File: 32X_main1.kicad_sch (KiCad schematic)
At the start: 17 parts, among them IC5041 315-5818-A, IC505 315-5805, IC509 74AC04

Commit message: Start PCB layout.
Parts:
- removed IC5041: 315-5818-A, symbol 32X:315-5818-A
- added IC504: 315-5818, Package_QFP:LQFP-176_24x24mm_P0.5mm, symbol 32X:315-5818
- C5: footprint (none) -> Capacitor_SMD:C_0805_2012Metric
- IC505: footprint (none) -> Package_QFP:PQFP-80_14x20mm_P0.8mm
- IC509: footprint (none) -> Package_SO:SO-14_3.9x8.65mm_P1.27mm
- R561, R562, R566: footprint (none) -> Resistor_SMD:R_0805_2012Metric
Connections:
- net CTD0: now also IC504.159 (RD0)
- net CTD1: now also IC504.160 (RD1)
- net CTD10: now also IC504.169 (RD10)
- net CTD11: now also IC504.170 (RD11)
- net CTD12: now also IC504.171 (RD12)
- net CTD13: now also IC504.172 (RD13)
- net CTD14: now also IC504.173 (RD14)
- net CTD15: now also IC504.174 (RD15)
- net CTD2: now also IC504.161 (RD2)
- net CTD3: now also IC504.162 (RD3)
- net CTD4: now also IC504.163 (RD4)
- net CTD5: now also IC504.164 (RD5)
- net CTD6: now also IC504.165 (RD6)
- net CTD7: now also IC504.166 (RD7)
- net CTD8: now also IC504.167 (RD8)
- net CTD9: now also IC504.168 (RD9)
- net GND: now also IC504.152 (CHPLL), IC504.153 (BUNRI), IC504.8 (KILL)
- net GNDA: now also IC504.130 (AGND)
- net PCH0: now also IC504.2 (CH0)
- net PCH1: now also IC504.3 (CH1)
- net VA1: now also IC504.84 (VA1)
- net VA10: now also IC504.75 (VA10)
- net VA11: now also IC504.74 (VA11)
- net VA12: now also IC504.73 (VA12)
- net VA13: now also IC504.72 (VA13)
- net VA14: now also IC504.71 (VA14)
- net VA15: now also IC504.70 (VA15)
- net VA16: now also IC504.69 (VA16)
- net VA17: now also IC504.68 (VA17)
- net VA18: now also IC504.67 (VA18)
- net VA19: now also IC504.101 (VA19)
- net VA2: now also IC504.83 (VA2)
- net VA20: now also IC504.102 (VA20)
- net VA21: now also IC504.103 (VA21)
- net VA22: now also IC504.104 (VA22)
- net VA23: now also IC504.105 (VA23)
- net VA3: now also IC504.82 (VA3)
- net VA4: now also IC504.81 (VA4)
- net VA5: now also IC504.80 (VA5)
- net VA6: now also IC504.79 (VA6)
- net VA7: now also IC504.78 (VA7)
- net VA8: now also IC504.77 (VA8)
- net VA9: now also IC504.76 (VA9)
- net VD0: now also IC504.86 (VD0)
- net VD1: now also IC504.92 (VD1)
- net VD10: now also IC504.96 (VD10)
- net VD11: now also IC504.99 (VD11)
- net VD12: now also IC504.117 (VD12)
- net VD13: now also IC504.116 (VD13)
- net VD14: now also IC504.115 (VD14)
- net VD15: now also IC504.114 (VD15)
- net VD2: now also IC504.95 (VD2)
- net VD3: now also IC504.98 (VD3)
- net VD4: now also IC504.97 (VD4)
- net VD5: now also IC504.94 (VD5)
- net VD6: now also IC504.91 (VD6)
- net VD7: now also IC504.85 (VD7)
- net VD8: now also IC504.90 (VD8)
- net VD9: now also IC504.93 (VD9)
- net ~{CART}: now also IC504.7 (~{CART})
- net ~{CAS0}: now also IC504.106 (~{CAS0})
- net ~{CAS2}: now also IC504.113 (~{CAS2})
- net ~{CASEL}: now also IC504.155 (~{OASEL})
- net ~{CCAS0}: now also IC504.157 (~{OCAS0})
- net ~{CCAS2}: now also IC504.156 (~{OCAS2})
- net ~{CCE0}: now also IC504.154 (~{OCE0})
- net ~{CE0}: now also IC504.107 (~{CE0})
- net ~{CLWR}: now also IC504.158 (~{OLWE})
- net ~{DTAK}: now also IC504.109 (~{DTAK})
- net ~{LWR}: now also IC504.120 (~{LWR})
- net ~{UWR}: now also IC504.121 (~{UWR})
- net ~{VRES}: now also IC504.119 (~{VRES})
- net ~{XRESET}: now also IC504.100 (~{MRES})
- net at FB7.2: now also IC504.108 (~{AS})
- net at FB7.2: now also IC504.112 (VCLK)
- net at FB7.2: now also IC504.118 (~{ASEL})
- net at C5.1, C5.1, L501.2: now also IC504.129 (AVDD)
- net at IC505.58 (~{SEL}): now also IC504.151 (~{SEL})
- net at FB7.1: now also IC504.33 (CKIO)
- net at IC505.10 (OVA19): now also IC504.4 (OVA19)
- net at IC505.9 (OVA20): now also IC504.5 (OVA20)
- net at IC505.8 (OVA21): now also IC504.6 (OVA21)
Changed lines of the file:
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@@
       (effects (font (size 1.27 1.27)) (justify right))
     )
-    (property "Footprint" "" (at 222.123 232.41 90)
+    (property "Footprint" "Resistor_SMD:R_0805_2012Metric" (at 222.123 232.41 90)
       (effects (font (size 1.27 1.27)) hide)
     )
@@
       (effects (font (size 1.27 1.27)))
     )
-    (property "Footprint" "" (at 135.89 237.49 0)
+    (property "Footprint" "Package_SO:SO-14_3.9x8.65mm_P1.27mm" (at 135.89 237.49 0)
       (effects (font (size 1.27 1.27)) hide)
     )
@@
     )
   )
-  (symbol (lib_id "32X:315-5818-A") (at 176.53 48.26 0) (unit 1)
-    (in_bom yes) (on_board yes) (dnp no)
-    (property "Reference" "IC5041" (at 176.53 43.815 0)
-      (effects (font (size 1.27 1.27)))
-    )
-    (property "Value" "315-5818-A" (at 176.53 46.355 0)
-      (effects (font (size 1.27 1.27)))
-    )
-    (property "Footprint" "" (at 176.53 83.82 0)
-      (effects (font (size 1.27 1.27)) hide)
-    )
-    (property "Datasheet" "" (at 176.53 83.82 0)
-      (effects (font (size 1.27 1.27)) hide)
-    )
-    (pin "100")
-    (pin "101")
-    (pin "102")
-    (pin "103")
-    (pin "104")
-    (pin "105")
-    (pin "106")
-    (pin "107")
-    (pin "108")
-    (pin "109")
-    (pin "112")
-    (pin "113")
-    (pin "114")
-    (pin "115")
-    (pin "116")
-    (pin "117")
-    (pin "118")
-    (pin "119")
-    (pin "120")
-    (pin "121")
-    (pin "128")
-    (pin "129")
-    (pin "130")
-    (pin "151")
-    (pin "152")
-    (pin "153")
-    (pin "154")
-    (pin "155")
-    (pin "156")
-    (pin "157")
-    (pin "158")
-    (pin "159")
-    (pin "160")
-    (pin "161")
-    (pin "162")
-    (pin "163")
-    (pin "164")
-    (pin "165")
-    (pin "166")
-    (pin "167")
-    (pin "168")
-    (pin "169")
-    (pin "170")
-    (pin "171")
-    (pin "172")
-    (pin "173")
-    (pin "174")
-    (pin "2")
-    (pin "3")
-    (pin "33")
-    (pin "4")
-    (pin "5")
-    (pin "6")
-    (pin "67")
-    (pin "68")
-    (pin "69")
-    (pin "7")
-    (pin "70")
-    (pin "71")
-    (pin "72")
-    (pin "73")
-    (pin "74")
-    (pin "75")
-    (pin "76")
-    (pin "77")
-    (pin "78")
-    (pin "79")
-    (pin "8")
-    (pin "80")
-    (pin "81")
-    (pin "82")
-    (pin "83")
-    (pin "84")
-    (pin "85")
-    (pin "86")
-    (pin "90")
-    (pin "91")
-    (pin "92")
-    (pin "93")
-    (pin "94")
-    (pin "95")
-    (pin "96")
-    (pin "97")
-    (pin "98")
-    (pin "99")
-    (instances
-      (project "Neptune"
-        (path "/bcc23b51-b742-4ae5-9dd6-d96a24058944/a9caee2e-423b-443e-a11f-5841882e2685"
-          (reference "IC5041") (unit 1)
-        )
-      )
-    )
-  )
   (symbol (lib_id "power:GND") (at 291.465 178.435 0) (unit 1)
     (in_bom yes) (on_board yes) (dnp no) (fields_autoplaced)
@@
       (effects (font (size 1.27 1.27)) (justify left))
     )
-    (property "Footprint" "" (at 257.81 251.46 0)
+    (property "Footprint" "Package_SO:SO-14_3.9x8.65mm_P1.27mm" (at 257.81 251.46 0)
       (effects (font (size 1.27 1.27)) hide)
     )
@@
       (effects (font (size 1.27 1.27)) (justify left))
     )
-    (property "Footprint" "" (at 195.9102 187.325 0)
+    (property "Footprint" "Capacitor_SMD:C_0805_2012Metric" (at 195.9102 187.325 0)
       (effects (font (size 1.27 1.27)) hide)
     )
@@
       (effects (font (size 1.27 1.27)) (justify left))
     )
-    (property "Footprint" "" (at 292.4302 165.1 0)
+    (property "Footprint" "Capacitor_SMD:C_0805_2012Metric" (at 292.4302 165.1 0)
       (effects (font (size 1.27 1.27)) hide)
     )
@@
       (effects (font (size 1.27 1.27)) (justify left))
     )
-    (property "Footprint" "" (at 273.3802 165.1 0)
+    (property "Footprint" "Capacitor_SMD:C_0805_2012Metric" (at 273.3802 165.1 0)
       (effects (font (size 1.27 1.27)) hide)
     )
@@
       (effects (font (size 1.27 1.27)) (justify left))
     )
-    (property "Footprint" "" (at 283.5402 165.1 0)
+    (property "Footprint" "Capacitor_SMD:C_0805_2012Metric" (at 283.5402 165.1 0)
       (effects (font (size 1.27 1.27)) hide)
     )
@@
       (effects (font (size 1.27 1.27)))
     )
-    (property "Footprint" "" (at 156.845 237.49 0)
+    (property "Footprint" "Package_SO:SO-14_3.9x8.65mm_P1.27mm" (at 156.845 237.49 0)
       (effects (font (size 1.27 1.27)) hide)
     )
@@
       (effects (font (size 1.27 1.27)))
     )
-    (property "Footprint" "" (at 118.11 156.845 0)
+    (property "Footprint" "Package_SO:SO-14_3.9x8.65mm_P1.27mm" (at 118.11 156.845 0)
       (effects (font (size 1.27 1.27)) hide)
     )
@@
       (effects (font (size 1.27 1.27)))
     )
-    (property "Footprint" "" (at 146.685 225.933 90)
+    (property "Footprint" "Resistor_SMD:R_0805_2012Metric" (at 146.685 225.933 90)
       (effects (font (size 1.27 1.27)) hide)
     )
@@
       (effects (font (size 1.27 1.27)))
     )
-    (property "Footprint" "" (at 117.475 239.268 90)
+    (property "Footprint" "Resistor_SMD:R_0805_2012Metric" (at 117.475 239.268 90)
       (effects (font (size 1.27 1.27)) hide)
     )
@@
       (effects (font (size 1.27 1.27)))
     )
-    (property "Footprint" "" (at 249.555 83.82 0)
+    (property "Footprint" "Package_QFP:PQFP-80_14x20mm_P0.8mm" (at 249.555 83.82 0)
       (effects (font (size 1.27 1.27)) hide)
     )
@@
       (effects (font (size 1.27 1.27)) (justify left))
     )
-    (property "Footprint" "" (at 204.8002 187.325 0)
+    (property "Footprint" "Capacitor_SMD:C_0805_2012Metric" (at 204.8002 187.325 0)
       (effects (font (size 1.27 1.27)) hide)
     )
@@
       (effects (font (size 1.27 1.27)))
     )
-    (property "Footprint" "" (at 249.555 203.2 0)
+    (property "Footprint" "Package_SO:SO-14_3.9x8.65mm_P1.27mm" (at 249.555 203.2 0)
       (effects (font (size 1.27 1.27)) hide)
     )
@@
         )
       )
+    )
+  )
+  (symbol (lib_id "32X:315-5818") (at 176.53 48.26 0) (unit 1)
+    (in_bom yes) (on_board yes) (dnp no) (fields_autoplaced)
+    (property "Reference" "IC504" (at 176.53 43.18 0)
+      (effects (font (size 1.27 1.27)))
+    )
+    (property "Value" "315-5818" (at 176.53 45.72 0)
+      (effects (font (size 1.27 1.27)))
+    )
+    (property "Footprint" "Package_QFP:LQFP-176_24x24mm_P0.5mm" (at 176.53 48.26 0)
+      (effects (font (size 1.27 1.27)) hide)
+    )
+    (property "Datasheet" "" (at 176.53 48.26 0)
+      (effects (font (size 1.27 1.27)) hide)
+    )
+    (pin "100")
+    (pin "101")
+    (pin "102")
+    (pin "103")
+    (pin "104")
+    (pin "105")
+    (pin "106")
+    (pin "107")
+    (pin "108")
+    (pin "109")
+    (pin "112")
+    (pin "113")
+    (pin "114")
+    (pin "115")
+    (pin "116")
+    (pin "117")
+    (pin "118")
+    (pin "119")
+    (pin "120")
+    (pin "121")
+    (pin "128")
+    (pin "129")
+    (pin "130")
+    (pin "151")
+    (pin "152")
+    (pin "153")
+    (pin "154")
+    (pin "155")
+    (pin "156")
+    (pin "157")
+    (pin "158")
+    (pin "159")
+    (pin "160")
+    (pin "161")
+    (pin "162")
+    (pin "163")
+    (pin "164")
+    (pin "165")
+    (pin "166")
+    (pin "167")
+    (pin "168")
+    (pin "169")
+    (pin "170")
+    (pin "171")
+    (pin "172")
+    (pin "173")
+    (pin "174")
+    (pin "2")
+    (pin "3")
+    (pin "33")
+    (pin "4")
+    (pin "5")
+    (pin "6")
+    (pin "67")
+    (pin "68")
+    (pin "69")
+    (pin "7")
+    (pin "70")
+    (pin "71")
+    (pin "72")
+    (pin "73")
+    (pin "74")
+    (pin "75")
+    (pin "76")
+    (pin "77")
+    (pin "78")
+    (pin "79")
+    (pin "8")
+    (pin "80")
+    (pin "81")
+    (pin "82")
+    (pin "83")
+    (pin "84")
+    (pin "85")
+    (pin "86")
+    (pin "90")
+    (pin "91")
+    (pin "92")
+    (pin "93")
+    (pin "94")
+    (pin "95")
+    (pin "96")
+    (pin "97")
+    (pin "98")
+    (pin "99")
+    (pin "1")
+    (pin "10")
+    (pin "11")
+    (pin "110")
+    (pin "111")
+    (pin "12")
+    (pin "122")
+    (pin "123")
+    (pin "124")
+    (pin "125")
+    (pin "126")
+    (pin "127")
+    (pin "13")
+    (pin "131")
+    (pin "132")
+    (pin "133")
+    (pin "134")
+    (pin "135")
+    (pin "136")
+    (pin "137")
+    (pin "138")
+    (pin "139")
+    (pin "14")
+    (pin "140")
+    (pin "141")
+    (pin "142")
+    (pin "143")
+    (pin "144")
+    (pin "145")
+    (pin "146")
+    (pin "147")
+    (pin "148")
+    (pin "149")
+    (pin "15")
+    (pin "150")
+    (pin "16")
+    (pin "17")
+    (pin "175")
+    (pin "176")
+    (pin "18")
+    (pin "19")
+    (pin "20")
+    (pin "21")
+    (pin "22")
+    (pin "23")
+    (pin "24")
+    (pin "25")
+    (pin "26")
+    (pin "27")
+    (pin "28")
+    (pin "29")
+    (pin "30")
+    (pin "31")
+    (pin "32")
+    (pin "34")
+    (pin "35")
+    (pin "36")
+    (pin "37")
+    (pin "38")
+    (pin "39")
+    (pin "40")
+    (pin "41")
+    (pin "42")
+    (pin "43")
+    (pin "44")
+    (pin "45")
+    (pin "46")
+    (pin "47")
+    (pin "48")
+    (pin "49")
+    (pin "50")
+    (pin "51")
+    (pin "52")
+    (pin "53")
+    (pin "54")
+    (pin "55")
+    (pin "56")
+    (pin "57")
+    (pin "58")
+    (pin "59")
+    (pin "60")
+    (pin "61")
+    (pin "62")
+    (pin "63")
+    (pin "64")
+    (pin "65")
+    (pin "66")
+    (pin "87")
+    (pin "88")
+    (pin "89")
+    (pin "9")
+    (instances
+      (project "Neptune"
+        (path "/bcc23b51-b742-4ae5-9dd6-d96a24058944/a9caee2e-423b-443e-a11f-5841882e2685"
+          (reference "IC504") (unit 1)
+        )
+      )

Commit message: Save first mock-up before updating footprints.
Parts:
- FB7, L501: footprint (none) -> Inductor_SMD:L_0805_2012Metric
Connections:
- net GND renamed GND2
- net GNDA renamed GNDA2
- net PCH0 renamed PCM0
- net PCH1 renamed PCM1

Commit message: Draft new layout with more accurate footprints.
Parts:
- C5: footprint Capacitor_SMD:C_0805_2012Metric -> Capacitor_SMD:C_1206_3216Metric
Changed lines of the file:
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@@
       (effects (font (size 1.27 1.27)) (justify left))
     )
-    (property "Footprint" "Capacitor_SMD:C_0805_2012Metric" (at 292.4302 165.1 0)
+    (property "Footprint" "Capacitor_SMD:C_1206_3216Metric" (at 292.4302 165.1 0)
       (effects (font (size 1.27 1.27)) hide)
     )
@@
       (effects (font (size 1.27 1.27)) (justify left))
     )
-    (property "Footprint" "Capacitor_SMD:C_0805_2012Metric" (at 204.8002 187.325 0)
-      (effects (font (size 1.27 1.27)) hide)
-    )
+    (property "Footprint" "Capacitor_SMD:C_1206_3216Metric" (at 204.8002 187.325 0)
+      (effects (font (size 1.27 1.27)) hide)
+    )

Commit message: Fill zones, DRC fixes.
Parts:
- added RM3, RM4, RM5, RM6: 4x10K, Resistor_SMD:R_Array_Convex_4x0603, symbol Device:R_Pack04
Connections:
- net GND2: now also RM3.1 (R1.1), RM3.2 (R2.1), RM3.3 (R3.1), RM3.4 (R4.1), RM4.1 (R1.1), RM4.2 (R2.1), RM4.3 (R3.1), RM4.4 (R4.1), RM5.1 (R1.1), RM5.2 (R2.1), RM5.3 (R3.1), RM5.4 (R4.1), RM6.1 (R1.1), RM6.2 (R2.1), RM6.3 (R3.1), RM6.4 (R4.1)
- net VD0: now also RM3.8 (R1.2)
- net VD1: now also RM3.7 (R2.2)
- net VD10: now also RM5.6 (R3.2)
- net VD11: now also RM5.5 (R4.2)
- net VD12: now also RM6.8 (R1.2)
- net VD13: now also RM6.7 (R2.2)
- net VD14: now also RM6.6 (R3.2)
- net VD15: now also RM6.5 (R4.2)
- net VD2: now also RM3.6 (R3.2)
- net VD3: now also RM3.5 (R4.2)
- net VD4: now also RM4.8 (R1.2)
- net VD5: now also RM4.7 (R2.2)
- net VD6: now also RM4.6 (R3.2)
- net VD7: now also RM4.5 (R4.2)
- net VD8: now also RM5.8 (R1.2)
- net VD9: now also RM5.7 (R2.2)

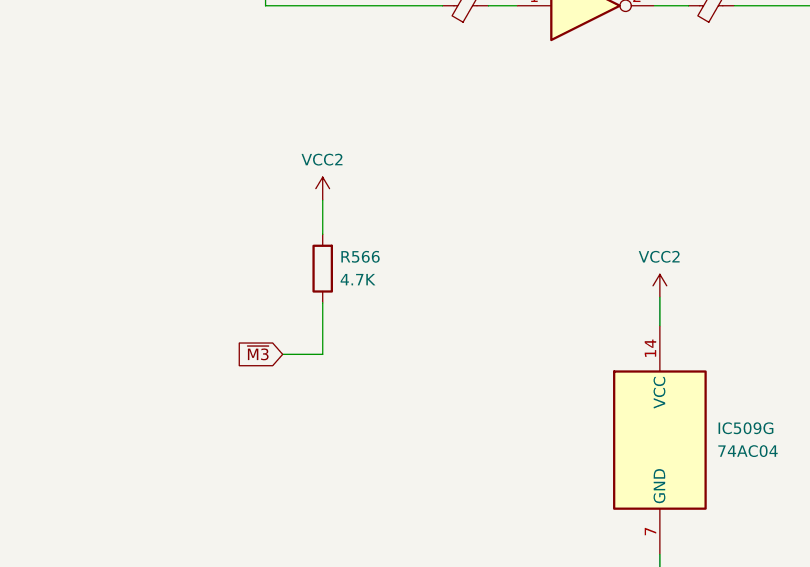
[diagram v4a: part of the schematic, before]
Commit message: Review/add 32X bodges.
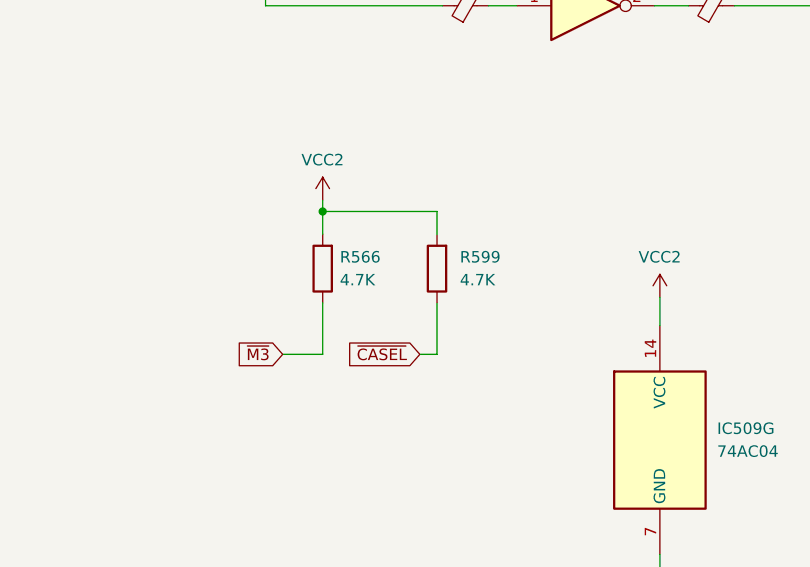
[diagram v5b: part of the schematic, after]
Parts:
- added R599: 4.7K, Resistor_SMD:R_0805_2012Metric, symbol Device:R
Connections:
- net VCC2: now also R599.2
- net ~{CASEL}: now also R599.1
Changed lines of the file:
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@@
   (junction (at 194.945 177.165) (diameter 0) (color 0 0 0 0)
+  )
+  (junction (at 220.345 226.06) (diameter 0) (color 0 0 0 0)
   )
   (junction (at 194.945 154.305) (diameter 0) (color 0 0 0 0)
@@
     (stroke (width 0) (type default))
   )
+  (wire (pts (xy 231.14 241.935) (xy 233.045 241.935))
+    (stroke (width 0) (type default))
+  )
   (bus (pts (xy 222.885 88.265) (xy 222.885 85.725))
     (stroke (width 0) (type default))
@@
     (stroke (width 0) (type default))
   )
-  (wire (pts (xy 220.345 224.79) (xy 220.345 228.6))
+  (wire (pts (xy 220.345 224.79) (xy 220.345 226.06))
     (stroke (width 0) (type default))
   )
@@
     (stroke (width 0) (type default))
   )
+  (wire (pts (xy 233.045 236.22) (xy 233.045 241.935))
+    (stroke (width 0) (type default))
+  )
   (wire (pts (xy 64.135 86.995) (xy 80.645 86.995))
     (stroke (width 0) (type default))
@@
     (stroke (width 0) (type default))
   )
+  (wire (pts (xy 233.045 226.06) (xy 233.045 228.6))
+    (stroke (width 0) (type default))
+  )
   (wire (pts (xy 234.315 55.245) (xy 225.425 55.245))
     (stroke (width 0) (type default))
@@
     (stroke (width 0) (type default))
   )
+  (wire (pts (xy 220.345 226.06) (xy 233.045 226.06))
+    (stroke (width 0) (type default))
+  )
   (wire (pts (xy 191.77 73.025) (xy 200.66 73.025))
     (stroke (width 0) (type default))
@@
   )
   (bus (pts (xy 137.795 101.6) (xy 142.24 101.6))
+    (stroke (width 0) (type default))
+  )
+  (wire (pts (xy 220.345 226.06) (xy 220.345 228.6))
     (stroke (width 0) (type default))
   )
@@
     (property "Intersheetrefs" "${INTERSHEET_REFS}" (at 285.3183 128.905 0)
       (effects (font (size 1.27 1.27)) (justify left) hide)
+    )
+  )
+  (global_label "~{CASEL}" (shape input) (at 231.14 241.935 180) (fields_autoplaced)
+    (effects (font (size 1.27 1.27)) (justify right))
+    (property "Intersheetrefs" "${INTERSHEET_REFS}" (at 222.4096 241.935 0)
+      (effects (font (size 1.27 1.27)) (justify right) hide)
     )
   )
@@
         )
       )
+    )
+  )
+  (symbol (lib_id "Device:R") (at 233.045 232.41 180) (unit 1)
+    (in_bom yes) (on_board yes) (dnp no) (fields_autoplaced)
+    (property "Reference" "R599" (at 235.585 231.14 0)
+      (effects (font (size 1.27 1.27)) (justify right))
+    )
+    (property "Value" "4.7K" (at 235.585 233.68 0)
+      (effects (font (size 1.27 1.27)) (justify right))
+    )
+    (property "Footprint" "Resistor_SMD:R_0805_2012Metric" (at 234.823 232.41 90)
+      (effects (font (size 1.27 1.27)) hide)
+    )
+    (property "Datasheet" "~" (at 233.045 232.41 0)
+      (effects (font (size 1.27 1.27)) hide)
+    )
+    (pin "1")
+    (pin "2")
+    (instances
+      (project "Neptune"
+        (path "/bcc23b51-b742-4ae5-9dd6-d96a24058944/a9caee2e-423b-443e-a11f-5841882e2685"
+          (reference "R599") (unit 1)
+        )
+      )

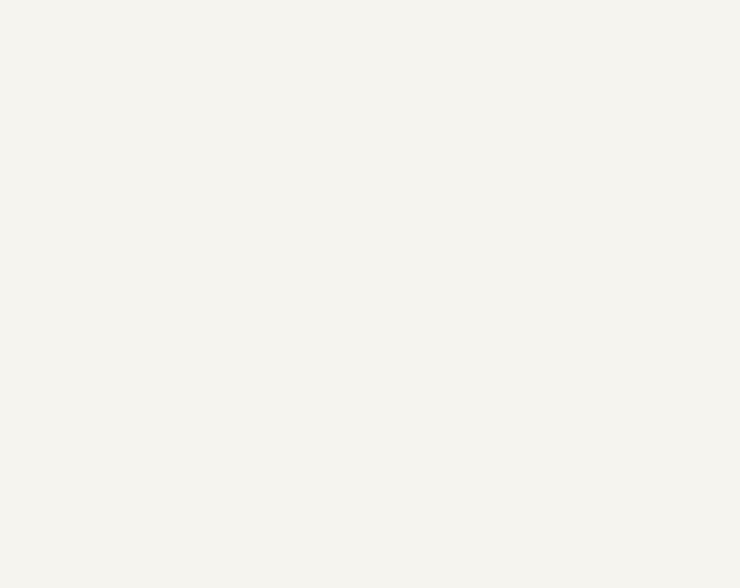
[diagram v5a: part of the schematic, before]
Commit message: Add missing/extra decoupling on 32X side.
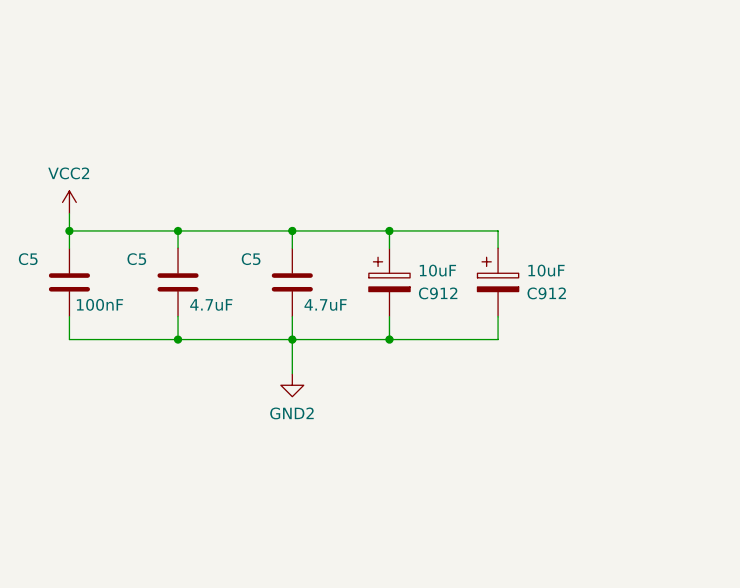
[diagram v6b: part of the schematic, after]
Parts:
- added C5: 100nF, Capacitor_SMD:C_0805_2012Metric, symbol Device:C
- added C5 (x2): 4.7uF, Capacitor_SMD:C_1206_3216Metric, symbol Device:C
- added C912 (x2): 10uF, Capacitor_THT:CP_Radial_D5.0mm_P2.50mm, symbol Device:C_Polarized
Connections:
- net GND2: now also C5.2, C5.2, C5.2, C912.2, C912.2
- net VCC2: now also C5.1, C5.1, C5.1, C912.1, C912.1
